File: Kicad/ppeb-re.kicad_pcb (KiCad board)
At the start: 2 copper layers, 115.7 x 56.4 mm, 34 parts, among them J1 TI-99_Sideport, J4 USB_A, P1 TI-99_Sideport, Q1 2N7002, Q2 2N7002, Q3 2N7002, SW1 SW_Push, U1 Pico, U2 ESP-PSRAM32, U3 74LVC245, U4 74LVC245, U5 74LVC245, U6 74HC138, U7 ESP-PSRAM32

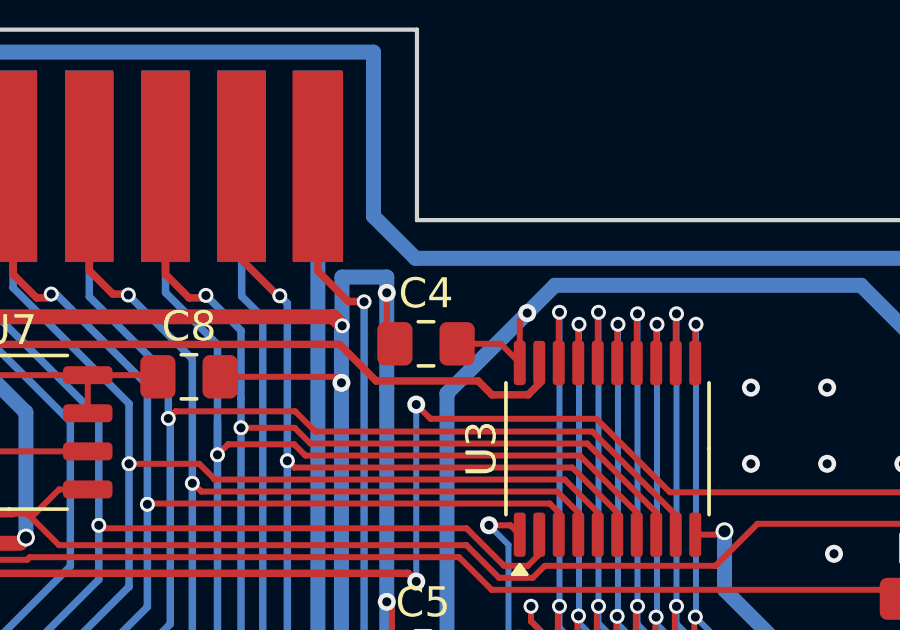
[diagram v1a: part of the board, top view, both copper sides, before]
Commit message: Remove c4 from board and schematic
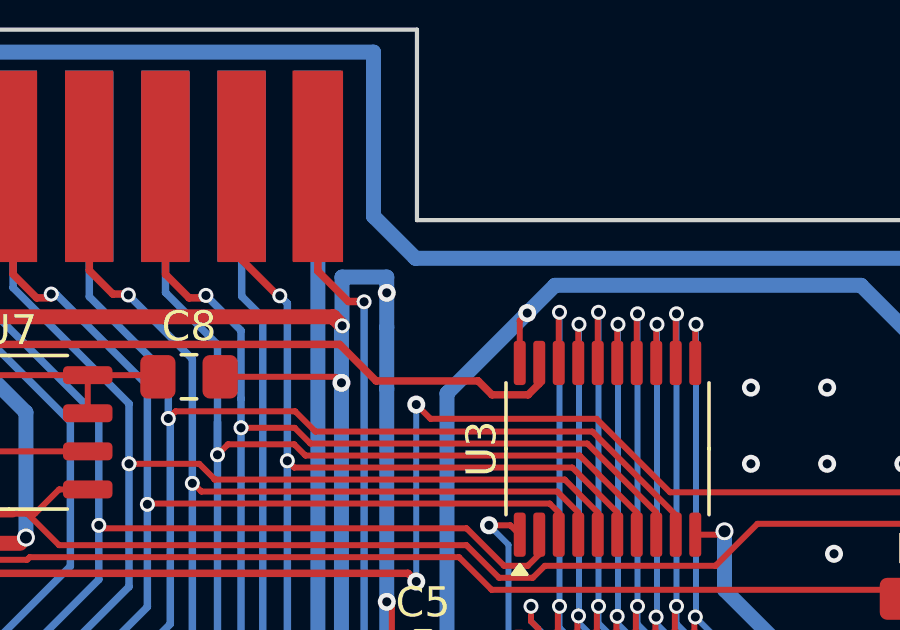
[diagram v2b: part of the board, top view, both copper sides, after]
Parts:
- removed C4: .1uf, Capacitor_SMD:C_0805_2012Metric_Pad1.18x1.45mm_HandSolder
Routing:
- net 3.3V: track 232.5 -> 230.1 mm
- net GND: track 764.7 -> 762.9 mm
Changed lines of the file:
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@@
 		)
 	)
-	(footprint "Capacitor_SMD:C_0805_2012Metric_Pad1.18x1.45mm_HandSolder"
-		(layer "F.Cu")
-		(at 182.9 59.5)
-		(descr "Capacitor SMD 0805 (2012 Metric), square (rectangular) end terminal, IPC_7351 nominal with elongated pad for handsoldering. (Body size source: IPC-SM-782 page 76, https://www.pcb-3d.com/wordpress/wp-content/uploads/ipc-sm-782a_amendment_1_and_2.pdf, https://docs.google.com/spreadsheets/d/1BsfQQcO9C6DZCsRaXUlFlo91Tg2WpOkGARC1WS5S8t0/edit?usp=sharing), generated with kicad-footprint-generator")
-		(tags "capacitor handsolder")
-		(property "Reference" "C4"
-			(at 0 -1.68 0)
-			(layer "F.SilkS")
-			(effects
-				(font
-					(size 1 1)
-					(thickness 0.15)
-				)
-			)
-		)
-		(property "Value" ".1uf"
-			(at 0 1.68 0)
-			(layer "F.Fab")
-			(effects
-				(font
-					(size 1 1)
-					(thickness 0.15)
-				)
-			)
-		)
-		(property "Footprint" "Capacitor_SMD:C_0805_2012Metric_Pad1.18x1.45mm_HandSolder"
-			(at 0 0 0)
-			(unlocked yes)
-			(layer "F.Fab")
-			(hide yes)
-			(effects
-				(font
-					(size 1.27 1.27)
-					(thickness 0.15)
-				)
-			)
-		)
-		(property "Datasheet" ""
-			(at 0 0 0)
-			(unlocked yes)
-			(layer "F.Fab")
-			(hide yes)
-			(effects
-				(font
-					(size 1.27 1.27)
-					(thickness 0.15)
-				)
-			)
-		)
-		(property "Description" "Unpolarized capacitor, small symbol"
-			(at 0 0 0)
-			(unlocked yes)
-			(layer "F.Fab")
-			(hide yes)
-			(effects
-				(font
-					(size 1.27 1.27)
-					(thickness 0.15)
-				)
-			)
-		)
-		(property "LCSC Part #" "C38141"
-			(at 0 0 0)
-			(unlocked yes)
-			(layer "F.Fab")
-			(hide yes)
-			(effects
-				(font
-					(size 1 1)
-					(thickness 0.15)
-				)
-			)
-		)
-		(property ki_fp_filters "C_*")
-		(sheetname "Root")
-		(sheetfile "ppeb-re.kicad_sch")
-		(attr smd exclude_from_bom dnp)
-		(fp_line
-			(start -0.261252 -0.735)
-			(end 0.261252 -0.735)
-			(stroke
-				(width 0.12)
-				(type solid)
-			)
-			(layer "F.SilkS")
-		)
-		(fp_line
-			(start -0.261252 0.735)
-			(end 0.261252 0.735)
-			(stroke
-				(width 0.12)
-				(type solid)
-			)
-			(layer "F.SilkS")
-		)
-		(fp_line
-			(start -1.88 -0.98)
-			(end 1.88 -0.98)
-			(stroke
-				(width 0.05)
-				(type solid)
-			)
-			(layer "F.CrtYd")
-		)
-		(fp_line
-			(start -1.88 0.98)
-			(end -1.88 -0.98)
-			(stroke
-				(width 0.05)
-				(type solid)
-			)
-			(layer "F.CrtYd")
-		)
-		(fp_line
-			(start 1.88 -0.98)
-			(end 1.88 0.98)
-			(stroke
-				(width 0.05)
-				(type solid)
-			)
-			(layer "F.CrtYd")
-		)
-		(fp_line
-			(start 1.88 0.98)
-			(end -1.88 0.98)
-			(stroke
-				(width 0.05)
-				(type solid)
-			)
-			(layer "F.CrtYd")
-		)
-		(fp_line
-			(start -1 -0.625)
-			(end 1 -0.625)
-			(stroke
-				(width 0.1)
-				(type solid)
-			)
-			(layer "F.Fab")
-		)
-		(fp_line
-			(start -1 0.625)
-			(end -1 -0.625)
-			(stroke
-				(width 0.1)
-				(type solid)
-			)
-			(layer "F.Fab")
-		)
-		(fp_line
-			(start 1 -0.625)
-			(end 1 0.625)
-			(stroke
-				(width 0.1)
-				(type solid)
-			)
-			(layer "F.Fab")
-		)
-		(fp_line
-			(start 1 0.625)
-			(end -1 0.625)
-			(stroke
-				(width 0.1)
-				(type solid)
-			)
-			(layer "F.Fab")
-		)
-		(fp_text user "${REFERENCE}"
-			(at 0 0 0)
-			(layer "F.Fab")
-			(effects
-				(font
-					(size 0.5 0.5)
-					(thickness 0.08)
-				)
-			)
-		)
-		(pad "1" smd roundrect
-			(at -1.0375 0)
-			(size 1.175 1.45)
-			(layers "F.Cu" "F.Paste" "F.Mask")
-			(roundrect_rratio 0.212766)
-			(net 1 "GND")
-			(pintype "passive")
-		)
-		(pad "2" smd roundrect
-			(at 1.0375 0)
-			(size 1.175 1.45)
-			(layers "F.Cu" "F.Paste" "F.Mask")
-			(roundrect_rratio 0.212766)
-			(net 2 "3.3V")
-			(pintype "passive")
-		)
-		(model "${KICAD8_3DMODEL_DIR}/Capacitor_SMD.3dshapes/C_0805_2012Metric.wrl"
-			(offset
-				(xyz 0 0 0)
-			)
-			(scale
-				(xyz 1 1 1)
-			)
-			(rotate
-				(xyz 0 0 0)
-			)
-		)
-	)
 	(footprint "Resistor_SMD:R_0805_2012Metric_Pad1.20x1.40mm_HandSolder"
 		(layer "F.Cu")
@@
 	)
 	(segment
-		(start 181.593145 57.8)
-		(end 181.593145 59.230645)
-		(width 0.2)
-		(layer "F.Cu")
-		(net 1)
-	)
-	(segment
 		(start 119.9 93.96728)
 		(end 119.85 94.01728)
@@
 	)
 	(segment
-		(start 181.593145 59.230645)
-		(end 181.8625 59.5)
-		(width 0.2)
-		(layer "F.Cu")
-		(net 1)
-	)
-	(segment
 		(start 181.7625 68.269355)
 		(end 181.593145 68.1)
@@
 	)
 	(segment
-		(start 185.3875 59.5)
-		(end 186.025 60.1375)
-		(width 0.2)
-		(layer "F.Cu")
-		(net 2)
-	)
-	(segment
 		(start 186.03125 75.45)
 		(end 184.76875 75.45)
@@
 		(layer "F.Cu")
 		(net 2)
-	)
-	(segment
-		(start 183.9375 59.5)
-		(end 185.3875 59.5)
-		(width 0.2)
-		(layer "F.Cu")
-		(net 2)

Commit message: Updated readme and silkscreen.
Update readme. Removed C4 from rear silkscreen.
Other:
- board text added: "C1 1uf C2 100uf C3 .1uf C5 .1uf C6 .1uf C7 .1uf C8 1uf"
- board text removed: "C1 1uf C2 100uf C3 .1uf C4 .1uf C5 .1uf C6 .1uf C7 .1uf C8 1uf"
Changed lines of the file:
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@@
 		)
 	)
-	(gr_text "C1 1uf\nC2 100uf\nC3 .1uf\nC4 .1uf\nC5 .1uf\nC6 .1uf\nC7 .1uf\nC8 1uf\n"
+	(gr_text "C1 1uf\nC2 100uf\nC3 .1uf\nC5 .1uf\nC6 .1uf\nC7 .1uf\nC8 1uf\n"
 		(at 192.5 82.5 0)
 		(layer "B.SilkS")
